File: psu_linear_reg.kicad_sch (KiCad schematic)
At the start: 24 parts, among them J1 Conn_Coaxial_Power, J2 Conn_Coaxial_Power, J3 Conn_01x10_Pin, J4 Conn_01x10_Pin, J5 Conn_01x10_Pin, J6 Conn_01x10_Pin, J7 Conn_01x05, J8 Conn_01x02, U1 L7805, U2 L7905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

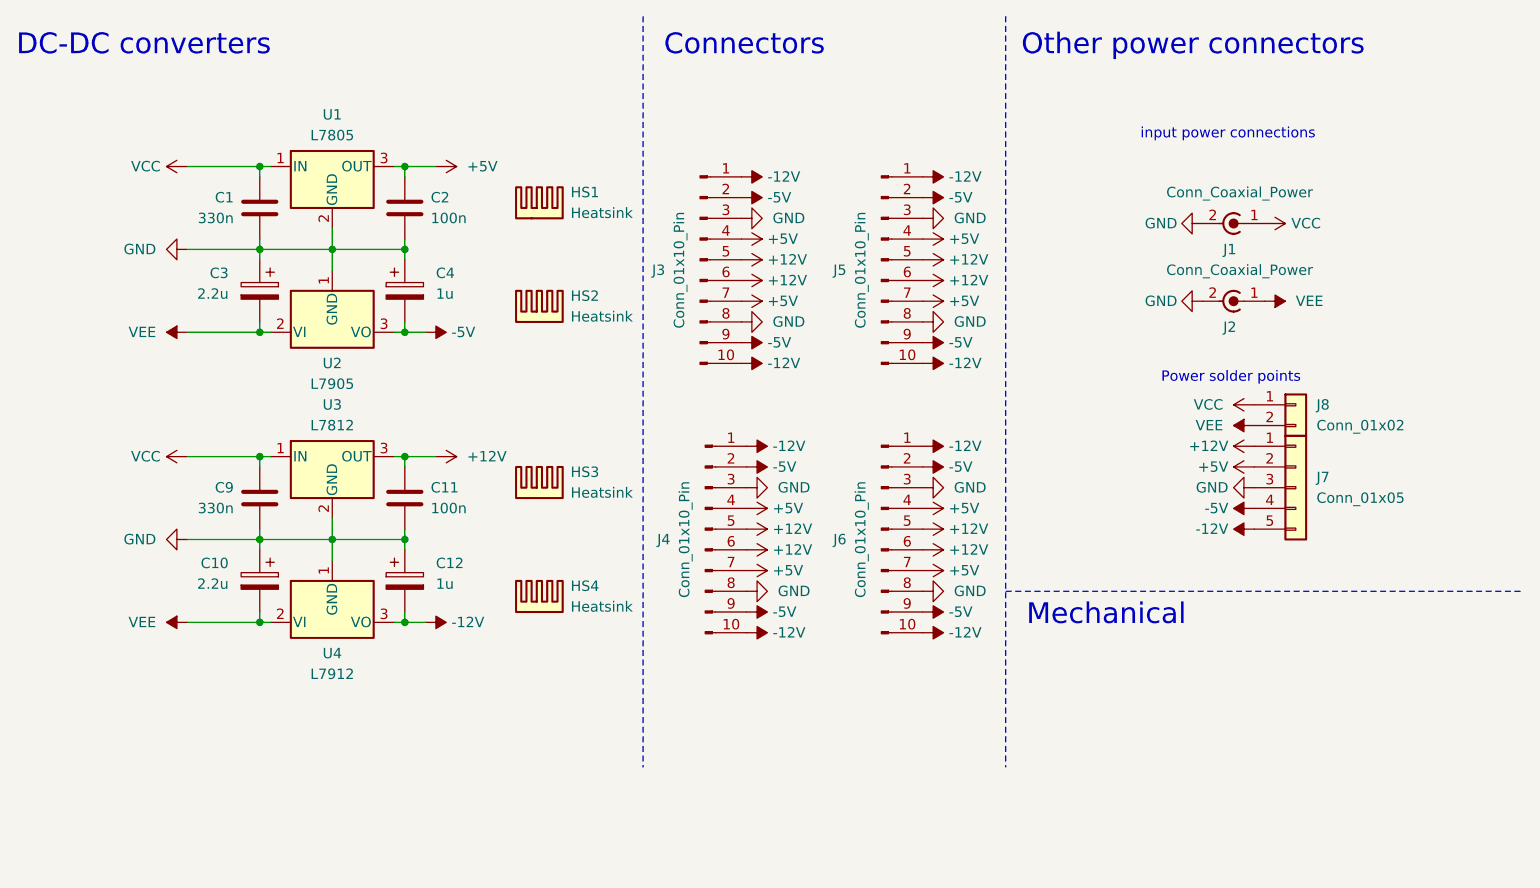
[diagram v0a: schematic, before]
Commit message: Added reverse polarity protection
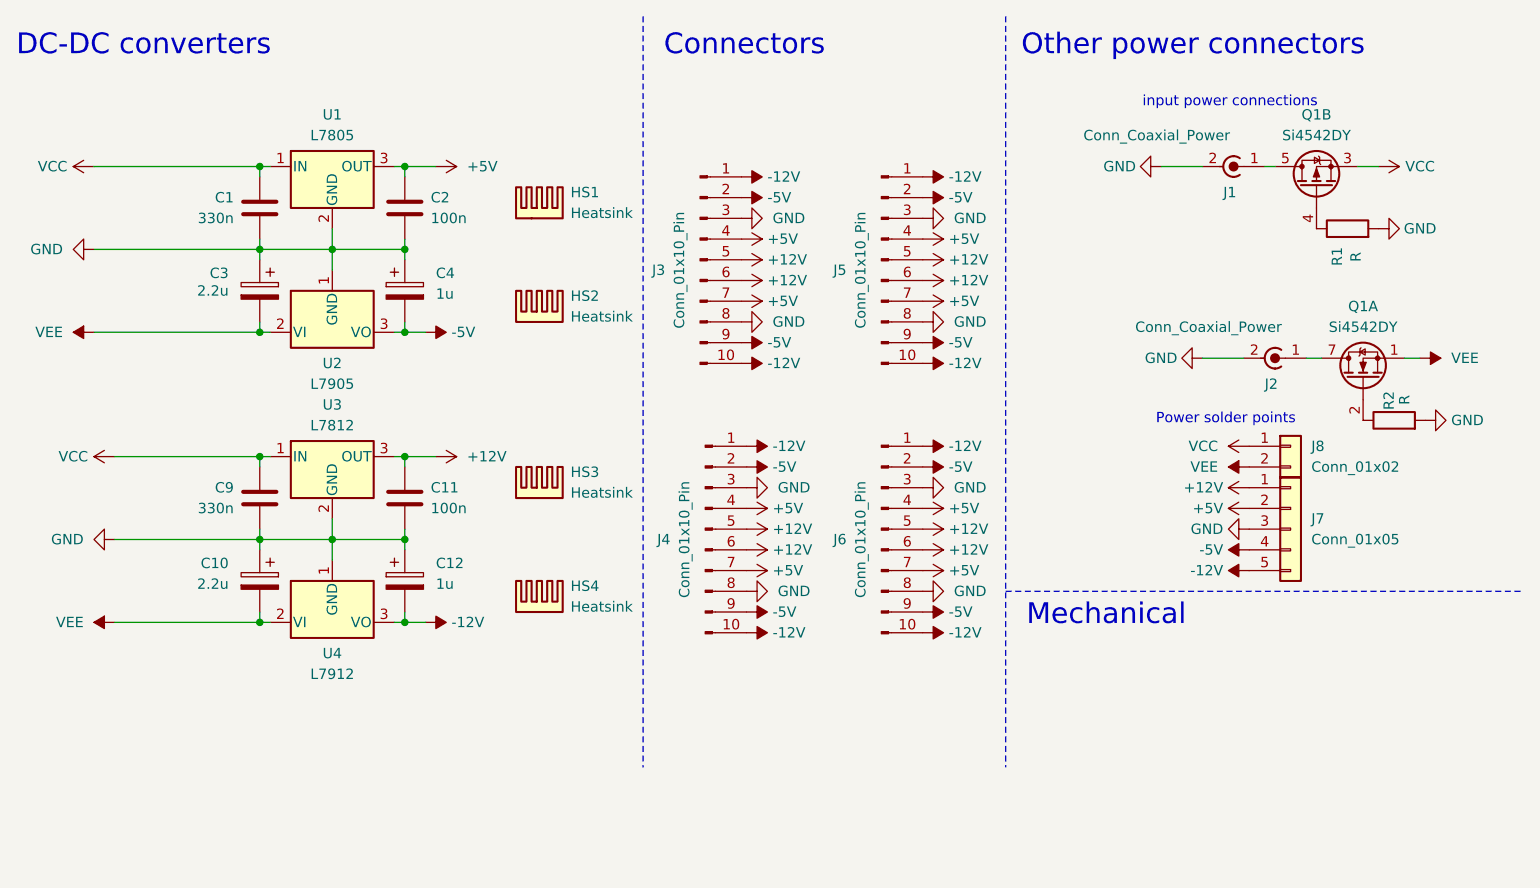
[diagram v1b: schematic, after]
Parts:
- added Q1: Si4542DY, Package_SO:SOIC-8_3.9x4.9mm_P1.27mm, symbol Transistor_FET:Si4542DY
- added R1, R2: R, symbol Device:R
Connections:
- net GND: now also R1.2, R2.2
- net VCC: now also Q1.3 (1); no longer J1.1 (In)
- net VEE: now also Q1.1 (S); no longer J2.1 (In)
- new net: Q1.2 (G), R2.1
- new net: J2.1 (In), Q1.7 (D), Q1.8 (D)
- new net: Q1.4 (G), R1.1
- new net: J1.1 (In), Q1.5 (D), Q1.6 (D)
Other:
- moved on the sheet: J1, J2, J7, J8

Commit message: Added reverse polarity protection. PCB ready for ordering
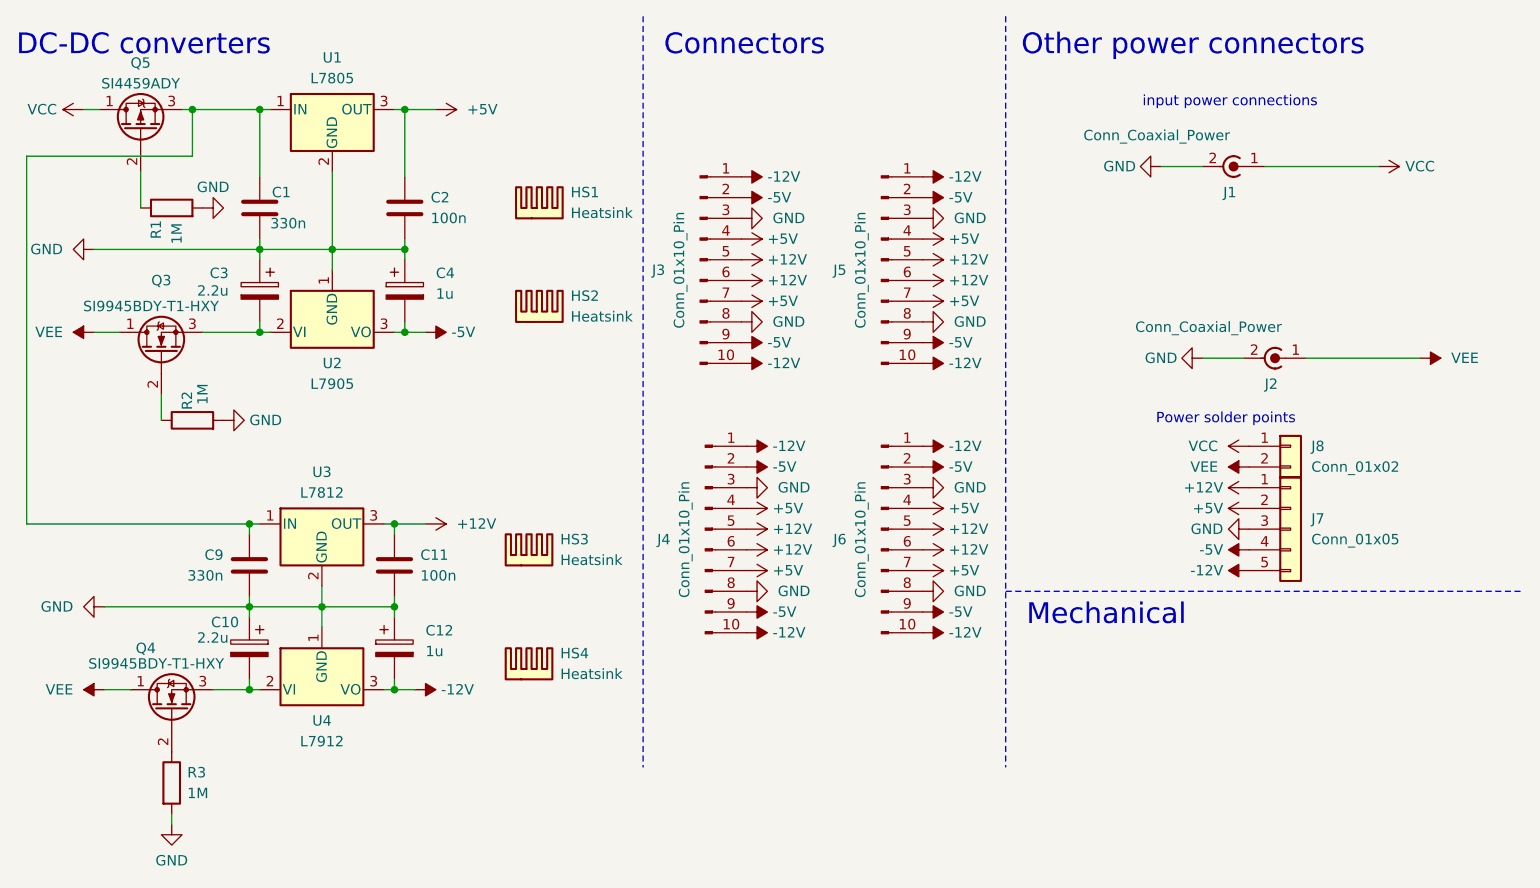
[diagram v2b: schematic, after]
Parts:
- removed Q1: Si4542DY, Package_SO:SOIC-8_3.9x4.9mm_P1.27mm, symbol Transistor_FET:Si4542DY
- added Q3, Q4: SI9945BDY-T1-HXY, Package_SO:SOP-8_3.76x4.96mm_P1.27mm, symbol Device:Q_NMOS_DGS
- added Q5: SI4459ADY, Package_SO:SOIC-8_3.9x4.9mm_P1.27mm, symbol Device:Q_PMOS_DGS
- added R3: 1M, Resistor_SMD:R_0603_1608Metric, symbol Device:R
- R1, R2: value R -> 1M; footprint (none) -> Resistor_SMD:R_0603_1608Metric
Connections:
- net GND: now also R3.2
- net VCC: now also J1.1 (In), Q5.1 (D); no longer C1.1, C9.1, U1.1 (IN), U3.1 (IN)
- net VEE: now also J2.1 (In), Q3.1 (D), Q4.1 (D); no longer C10.2, C3.2, U2.2 (VI), U4.2 (VI)
- net at R2.1: now also Q3.2 (G)
- net at R1.1: now also Q5.2 (G)
- new net: C3.2, Q3.3 (S), U2.2 (VI)
- new net: C10.2, Q4.3 (S), U4.2 (VI)
- new net: C1.1, C9.1, Q5.3 (S), U1.1 (IN), U3.1 (IN)
- new net: Q4.2 (G), R3.1
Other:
- moved on the sheet: C10, C11, C12, C9, HS3, HS4, U1, U3, U4

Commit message: rev 1.2. Fixed negative supply nmos protection
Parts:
- removed Q3, Q4: SI9945BDY-T1-HXY, Package_SO:SOP-8_3.76x4.96mm_P1.27mm, symbol Device:Q_NMOS_DGS
- added Q1, Q2: AO3400A, Package_TO_SOT_SMD:SOT-23, symbol Transistor_FET:AO3400A
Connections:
- net VEE: now also Q1.3 (D), Q2.3 (D)
- net at C3.2, U2.2 (VI): now also Q1.2 (S)
- net at R2.1: now also Q1.1 (G)
- net at C10.2, U4.2 (VI): now also Q2.2 (S)
- net at R3.1: now also Q2.1 (G)
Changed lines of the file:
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@@
 	)
 	(symbol
-		(lib_id "Device:Q_NMOS_DGS")
-		(at 31.115 53.34 90)
-		(unit 1)
-		(exclude_from_sim no)
-		(in_bom yes)
-		(on_board yes)
-		(dnp no)
-		(property "Reference" "Q3"
-			(at 31.115 44.45 90)
-			(effects
-				(font
-					(size 1.27 1.27)
-				)
-			)
-		)
-		(property "Value" "SI9945BDY-T1-HXY"
-			(at 29.845 47.625 90)
-			(effects
-				(font
-					(size 1.27 1.27)
-				)
-			)
-		)
-		(property "Footprint" "Package_SO:SOP-8_3.76x4.96mm_P1.27mm"
-			(at 28.575 48.26 0)
-			(effects
-				(font
-					(size 1.27 1.27)
-				)
-				(hide yes)
-			)
-		)
-		(property "Datasheet" "~"
-			(at 31.115 53.34 0)
-			(effects
-				(font
-					(size 1.27 1.27)
-				)
-				(hide yes)
-			)
-		)
-		(property "Description" "N-MOSFET transistor, drain/gate/source"
-			(at 31.115 53.34 0)
-			(effects
-				(font
-					(size 1.27 1.27)
-				)
-				(hide yes)
-			)
-		)
-		(pin "2"
-		)
-		(pin "1"
-		)
-		(pin "3"
-		)
-		(instances
-			(project ""
-				(path "/9c6abd11-1aac-4f08-8b79-cac116854bcb"
-					(reference "Q3")
-					(unit 1)
-				)
-			)
-		)
-	)
-	(symbol
 		(lib_id "power:VEE")
 		(at 164.465 67.31 90)
@@
 	)
 	(symbol
+		(lib_id "Transistor_FET:AO3400A")
+		(at 32.385 97.155 90)
+		(unit 1)
+		(exclude_from_sim no)
+		(in_bom yes)
+		(on_board yes)
+		(dnp no)
+		(fields_autoplaced yes)
+		(property "Reference" "Q2"
+			(at 32.385 88.265 90)
+			(effects
+				(font
+					(size 1.27 1.27)
+				)
+			)
+		)
+		(property "Value" "AO3400A"
+			(at 32.385 90.805 90)
+			(effects
+				(font
+					(size 1.27 1.27)
+				)
+			)
+		)
+		(property "Footprint" "Package_TO_SOT_SMD:SOT-23"
+			(at 34.29 92.075 0)
+			(effects
+				(font
+					(size 1.27 1.27)
+					(italic yes)
+				)
+				(justify left)
+				(hide yes)
+			)
+		)
+		(property "Datasheet" "http://www.aosmd.com/pdfs/datasheet/AO3400A.pdf"
+			(at 36.195 92.075 0)
+			(effects
+				(font
+					(size 1.27 1.27)
+				)
+				(justify left)
+				(hide yes)
+			)
+		)
+		(property "Description" "30V Vds, 5.7A Id, N-Channel MOSFET, SOT-23"
+			(at 32.385 97.155 0)
+			(effects
+				(font
+					(size 1.27 1.27)
+				)
+				(hide yes)
+			)
+		)
+		(property "JLCPCB PN" "C347475"
+			(at 32.385 97.155 0)
+			(effects
+				(font
+					(size 1.27 1.27)
+				)
+				(hide yes)
+			)
+		)
+		(pin "1"
+		)
+		(pin "2"
+		)
+		(pin "3"
+		)
+		(instances
+			(project "psu_linear_reg"
+				(path "/9c6abd11-1aac-4f08-8b79-cac116854bcb"
+					(reference "Q2")
+					(unit 1)
+				)
+			)
+		)
+	)
+	(symbol
 		(lib_id "power:-12V")
 		(at 62.23 94.615 270)
@@
 	)
 	(symbol
-		(lib_id "Device:Q_NMOS_DGS")
-		(at 32.385 97.155 90)
-		(unit 1)
-		(exclude_from_sim no)
-		(in_bom yes)
-		(on_board yes)
-		(dnp no)
-		(property "Reference" "Q4"
-			(at 29.21 89.535 90)
-			(effects
-				(font
-					(size 1.27 1.27)
-				)
-			)
-		)
-		(property "Value" "SI9945BDY-T1-HXY"
-			(at 30.48 91.44 90)
-			(effects
-				(font
-					(size 1.27 1.27)
-				)
-			)
-		)
-		(property "Footprint" "Package_SO:SOP-8_3.76x4.96mm_P1.27mm"
-			(at 29.845 92.075 0)
-			(effects
-				(font
-					(size 1.27 1.27)
-				)
-				(hide yes)
-			)
-		)
-		(property "Datasheet" "~"
-			(at 32.385 97.155 0)
-			(effects
-				(font
-					(size 1.27 1.27)
-				)
-				(hide yes)
-			)
-		)
-		(property "Description" "N-MOSFET transistor, drain/gate/source"
-			(at 32.385 97.155 0)
-			(effects
-				(font
-					(size 1.27 1.27)
-				)
-				(hide yes)
-			)
-		)
-		(pin "2"
-		)
-		(pin "1"
-		)
-		(pin "3"
-		)
-		(instances
-			(project "psu_linear_reg"
-				(path "/9c6abd11-1aac-4f08-8b79-cac116854bcb"
-					(reference "Q4")
-					(unit 1)
-				)
-			)
-		)
-	)
-	(symbol
 		(lib_id "power:+5V")
 		(at 64.77 23.495 270)
@@
 					(unit 1)
 				)
+			)
+		)
+	)
+	(symbol
+		(lib_id "Transistor_FET:AO3400A")
+		(at 31.115 53.34 90)
+		(unit 1)
+		(exclude_from_sim no)
+		(in_bom yes)
+		(on_board yes)
+		(dnp no)
+		(fields_autoplaced yes)
+		(property "Reference" "Q1"
+			(at 31.115 44.45 90)
+			(effects
+				(font
+					(size 1.27 1.27)
+				)
+			)
+		)
+		(property "Value" "AO3400A"
+			(at 31.115 46.99 90)
+			(effects
+				(font
+					(size 1.27 1.27)
+				)
+			)
+		)
+		(property "Footprint" "Package_TO_SOT_SMD:SOT-23"
+			(at 33.02 48.26 0)
+			(effects
+				(font
+					(size 1.27 1.27)
+					(italic yes)
+				)
+				(justify left)
+				(hide yes)
+			)
+		)
+		(property "Datasheet" "http://www.aosmd.com/pdfs/datasheet/AO3400A.pdf"
+			(at 34.925 48.26 0)
+			(effects
+				(font
+					(size 1.27 1.27)
+				)
+				(justify left)
+				(hide yes)
+			)
+		)
+		(property "Description" "30V Vds, 5.7A Id, N-Channel MOSFET, SOT-23"
+			(at 31.115 53.34 0)
+			(effects
+				(font
+					(size 1.27 1.27)
+				)
+				(hide yes)
+			)
+		)
+		(property "JLCPCB PN" "C347475"
+			(at 31.115 53.34 0)
+			(effects
+				(font
+					(size 1.27 1.27)
+				)
+				(hide yes)
+			)
+		)
+		(pin "1"
+		)
+		(pin "2"
+		)
+		(pin "3"
+		)
+		(instances
+			(project ""
+				(path "/9c6abd11-1aac-4f08-8b79-cac116854bcb"
+					(reference "Q1")
+					(unit 1)
+				)
